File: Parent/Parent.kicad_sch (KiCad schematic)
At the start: 0 parts

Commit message: Worked on Parent - Move Workspace to cloud
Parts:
- added BT105, BT29, BT30, BT45, BT60, BT75, BT90: Battery_Cell, symbol Device:Battery_Cell
- added D1, D2, D3, D4, D5, D6, D7, D8: LED, symbol Device:LED
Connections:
- net Fuse Box/Lights Back Fused: now also D1.2 (A), D2.2 (A), D4.2 (A), D6.2 (A), D8.2 (A)
- net Fuse Box/Lights Front Fused: now also D3.2 (A), D5.2 (A), D7.2 (A)
- new net -BATT: BT29.2 (-)
- new net BMS_Passive1/Batt+: BT29.1 (+), BT30.2 (-)
- new net BMS_Passive2/Batt+: BT30.1 (+), BT45.2 (-)
- new net BMS_Passive3/Batt+: BT45.1 (+), BT60.2 (-)
- new net BMS_Passive4/Batt+: BT60.1 (+), BT75.2 (-)
- new net BMS_Passive5/Batt+: BT75.1 (+), BT90.2 (-)
- new net BMS_Passive6/Batt+: BT105.2 (-), BT90.1 (+)
- new net BMS_Passive7/Batt+: BT105.1 (+)
- new net Lights Controller/BrakeDrain_{S0}: D1.1 (K)
- new net Lights Controller/BrakeDrain_{S1}: D2.1 (K)
- new net Lights Controller/HazzardDrain_{L}: D5.1 (K), D6.1 (K)
- new net Lights Controller/HazzardDrain_{R}: D7.1 (K), D8.1 (K)
- new net Lights Controller/MainDrain: D3.1 (K), D4.1 (K)
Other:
- removed sheet BMS
- added sheet BMS_Passive1 (BMS_Passive.kicad_sch)
- added sheet BMS_Passive2 (BMS_Passive.kicad_sch)
- added sheet BMS_Passive3 (BMS_Passive.kicad_sch)
- added sheet BMS_Passive4 (BMS_Passive.kicad_sch)
- added sheet BMS_Passive5 (BMS_Passive.kicad_sch)
- added sheet BMS_Passive6 (BMS_Passive.kicad_sch)
- added sheet BMS_Passive7 (BMS_Passive.kicad_sch)
- added sheet Battery Charger (BatteryCharger.kicad_sch)
- added sheet Fault Logic Controller (FaultLogicController.kicad_sch)
- added sheet Level Translator1 (LevelTranslator.kicad_sch)
- added sheet Level Translator2 (LevelTranslator.kicad_sch)
- added sheet Level Translator3 (LevelTranslator.kicad_sch)
- added sheet Level Translator4 (LevelTranslator.kicad_sch)
- added sheet Level Translator5 (LevelTranslator.kicad_sch)
- added sheet Level Translator6 (LevelTranslator.kicad_sch)
- added sheet Level Translator7 (LevelTranslator.kicad_sch)
- added sheet Lights Controller (Light Controller.kicad_sch)
- sheet Fuse Box ports: added Battery Charger ; removed none
- note added: "Battery Charger"

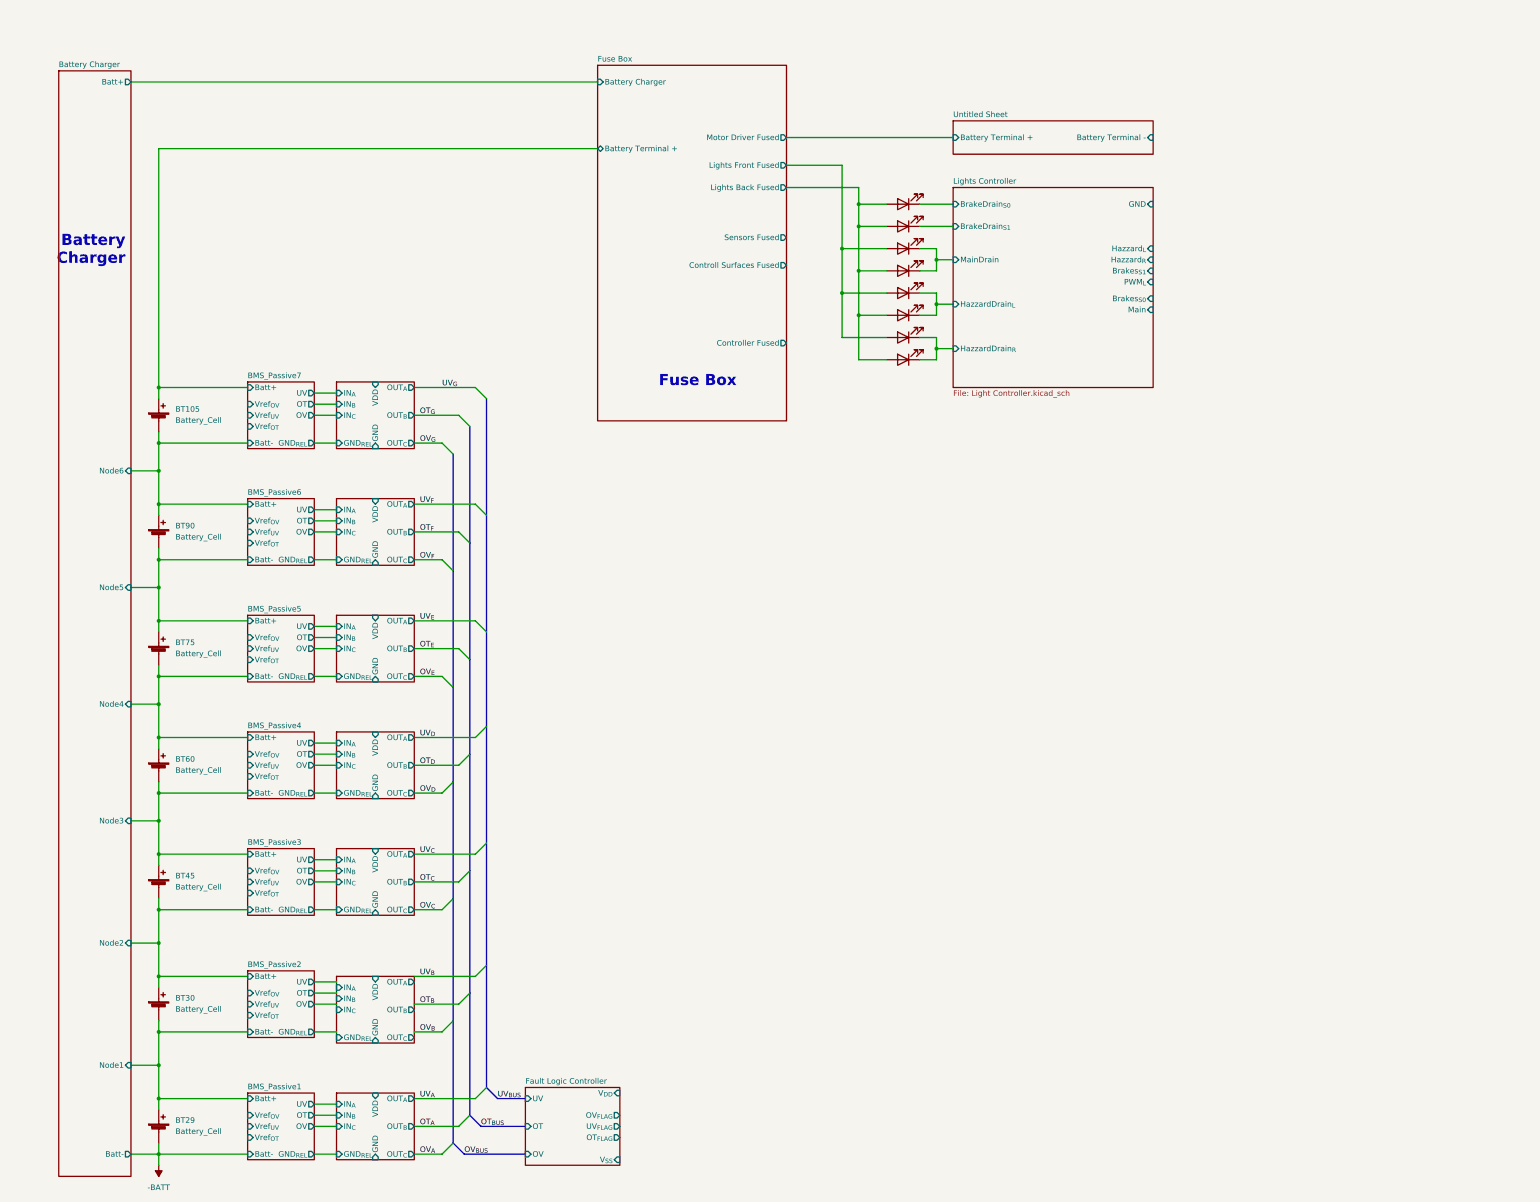
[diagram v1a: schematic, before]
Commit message: Updated Parent further - Move workspace to cloud
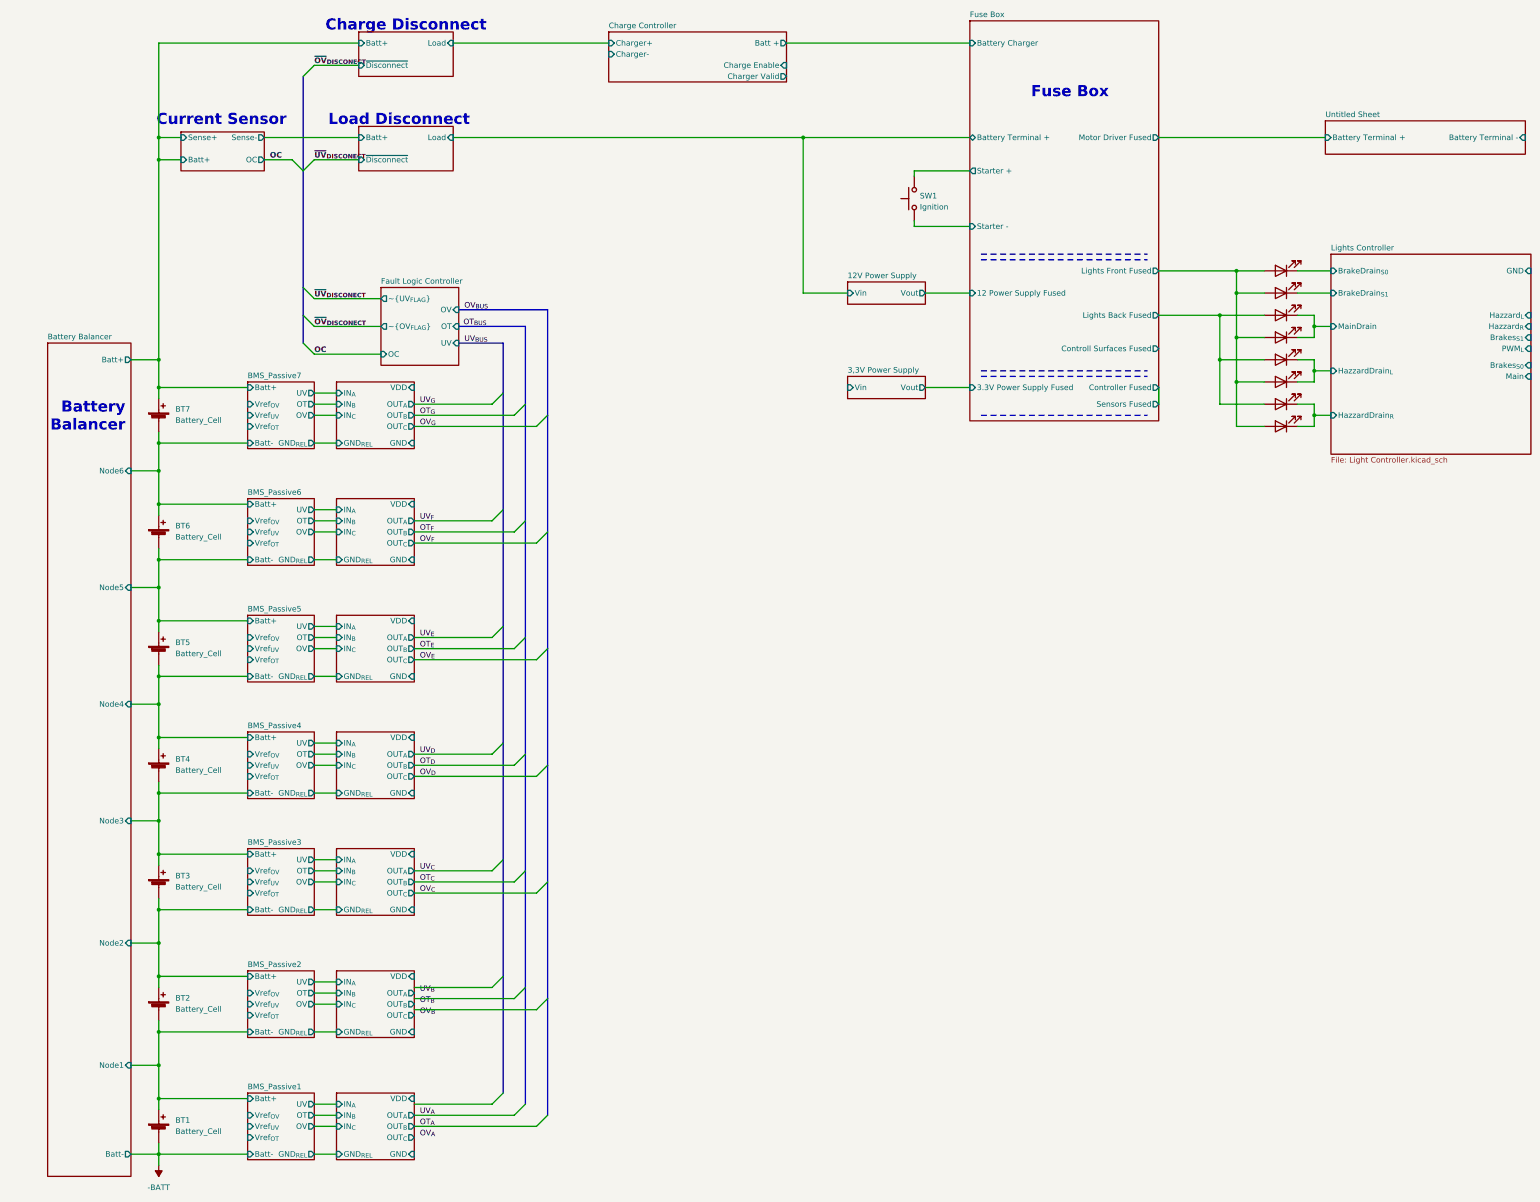
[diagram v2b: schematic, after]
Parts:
- added SW1: Ignition, symbol Switch:SW_Push
- renumbered BT29 to BT1, BT30 to BT2, BT45 to BT3, BT60 to BT4, BT75 to BT5, BT90 to BT6, BT105 to BT7
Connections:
- net Fuse Box/Lights Back Fused: now also D3.2 (A), D5.2 (A), D7.2 (A); no longer D1.2 (A), D2.2 (A), D4.2 (A), D6.2 (A), D8.2 (A)
- net Fuse Box/Lights Front Fused: now also D1.2 (A), D2.2 (A), D4.2 (A), D6.2 (A), D8.2 (A); no longer D3.2 (A), D5.2 (A), D7.2 (A)
- new net Fuse Box/Starter +: SW1.2
- new net Fuse Box/Starter -: SW1.1
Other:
- sheet Battery Charger renamed Battery Balancer
- added sheet 12V Power Supply (12V_PowerSupply.kicad_sch)
- added sheet 3,3V Power Supply (3.3V_PowerSupply.kicad_sch)
- added sheet Charge Controller (ChargeController.kicad_sch)
- added sheet Disconnect  (LoadStop_sch.kicad_sch)
- added sheet Overcurrent Detection (OvercurrentDetection.kicad_sch)
- sheet Fault Logic Controller ports: added OC, ~{OV_{FLAG}}, ~{UV_{FLAG}}; removed OT_{FLAG}, OV_{FLAG}, UV_{FLAG}, V_{DD}, V_{SS}
- sheet Fuse Box ports: added 12 Power Supply Fused, 3.3V Power Supply Fused, Starter +, Starter -; removed none
- note added: "Battery Balancer"
- note added: "Charge Disconnect"
- note added: "Current Sensor"
- note added: "Load Disconnect"
- note removed: "Battery Charger"

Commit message: Updated Parent further - Move workspace to cloud
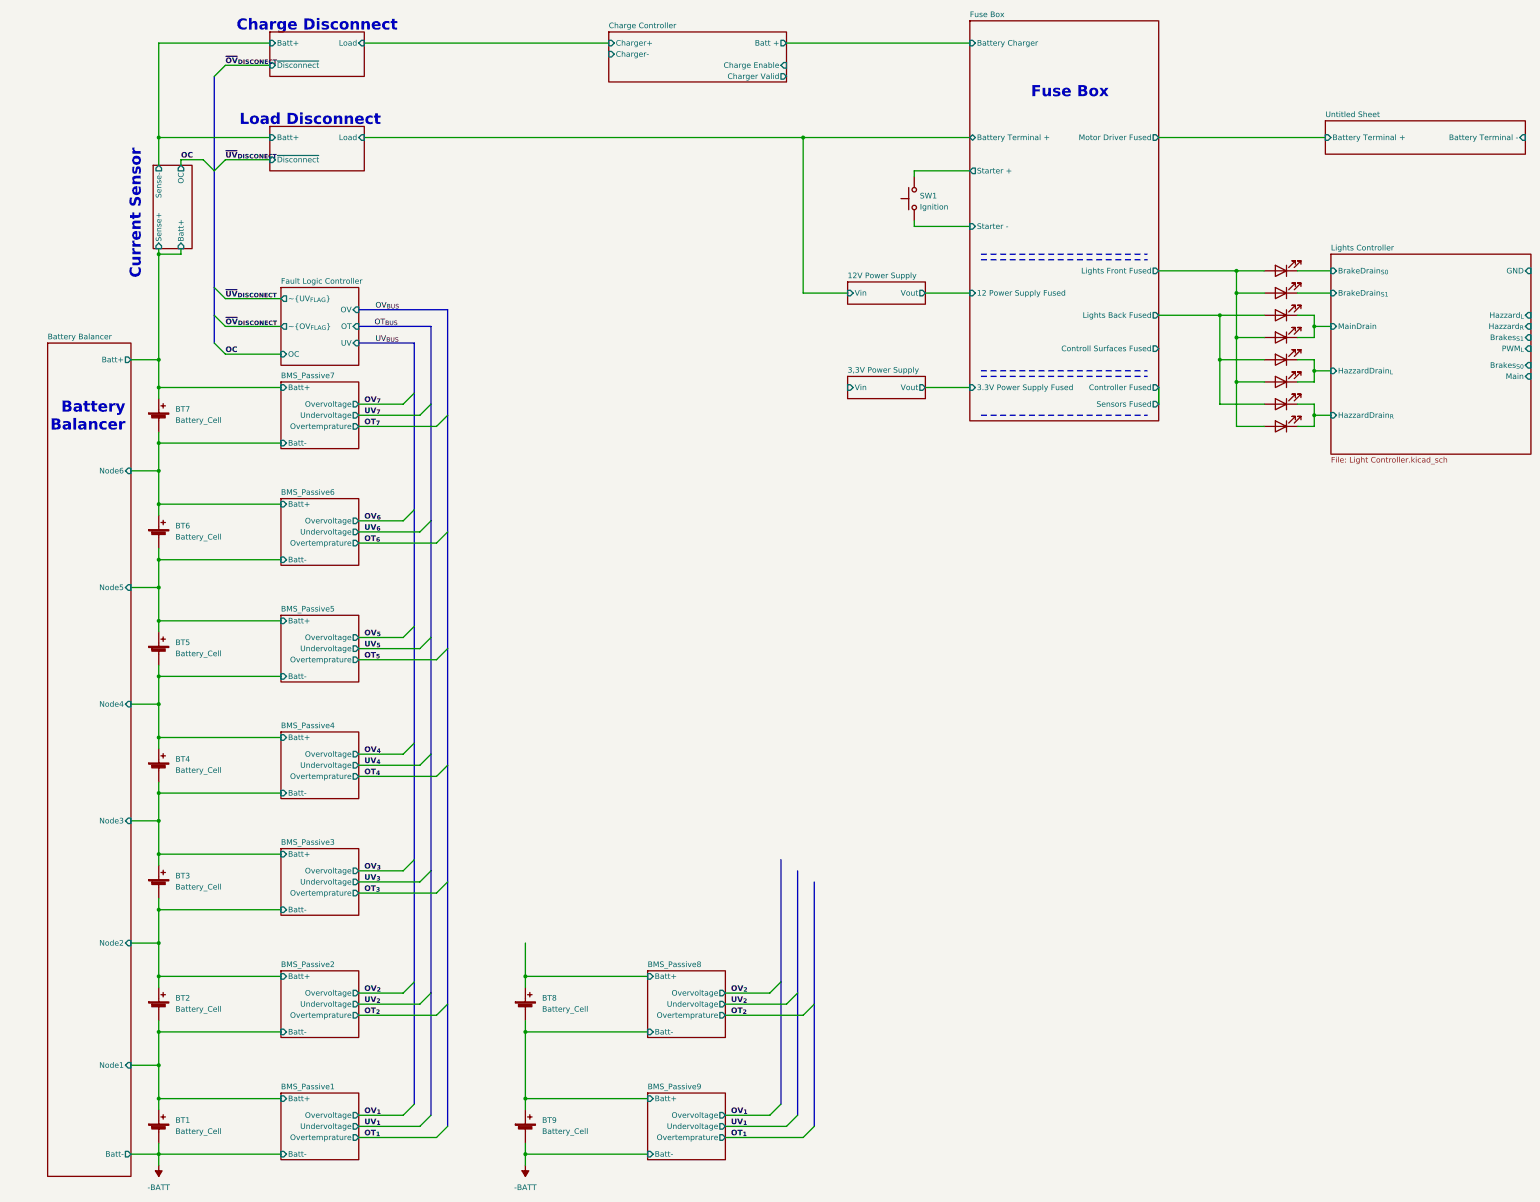
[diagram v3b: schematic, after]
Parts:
- added BT8, BT9: Battery_Cell, symbol Device:Battery_Cell
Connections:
- net -BATT: now also BT9.2 (-)
- new net BMS_Passive8/Batt+: BT8.1 (+)
- new net BMS_Passive8/Batt-: BT8.2 (-), BT9.1 (+)
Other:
- removed sheet Level Translator1
- removed sheet Level Translator2
- removed sheet Level Translator3
- removed sheet Level Translator4
- removed sheet Level Translator5
- removed sheet Level Translator6
- removed sheet Level Translator7
- added sheet BMS_Passive8 (BMS_Passive.kicad_sch)
- added sheet BMS_Passive9 (BMS_Passive.kicad_sch)
- sheet BMS_Passive1 ports: added Overtemprature, Overvoltage, Undervoltage; removed GND_{REL}, OT, OV, UV, Vref_{OT}, Vref_{OV}, Vref_{UV}
- sheet BMS_Passive2 ports: added Overtemprature, Overvoltage, Undervoltage; removed GND_{REL}, OT, OV, UV, Vref_{OT}, Vref_{OV}, Vref_{UV}
- sheet BMS_Passive3 ports: added Overtemprature, Overvoltage, Undervoltage; removed GND_{REL}, OT, OV, UV, Vref_{OT}, Vref_{OV}, Vref_{UV}
- sheet BMS_Passive4 ports: added Overtemprature, Overvoltage, Undervoltage; removed GND_{REL}, OT, OV, UV, Vref_{OT}, Vref_{OV}, Vref_{UV}
- sheet BMS_Passive5 ports: added Overtemprature, Overvoltage, Undervoltage; removed GND_{REL}, OT, OV, UV, Vref_{OT}, Vref_{OV}, Vref_{UV}
- sheet BMS_Passive6 ports: added Overtemprature, Overvoltage, Undervoltage; removed GND_{REL}, OT, OV, UV, Vref_{OT}, Vref_{OV}, Vref_{UV}
- sheet BMS_Passive7 ports: added Overtemprature, Overvoltage, Undervoltage; removed GND_{REL}, OT, OV, UV, Vref_{OT}, Vref_{OV}, Vref_{UV}

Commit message: Updated Parent - Moved workspace to cloud
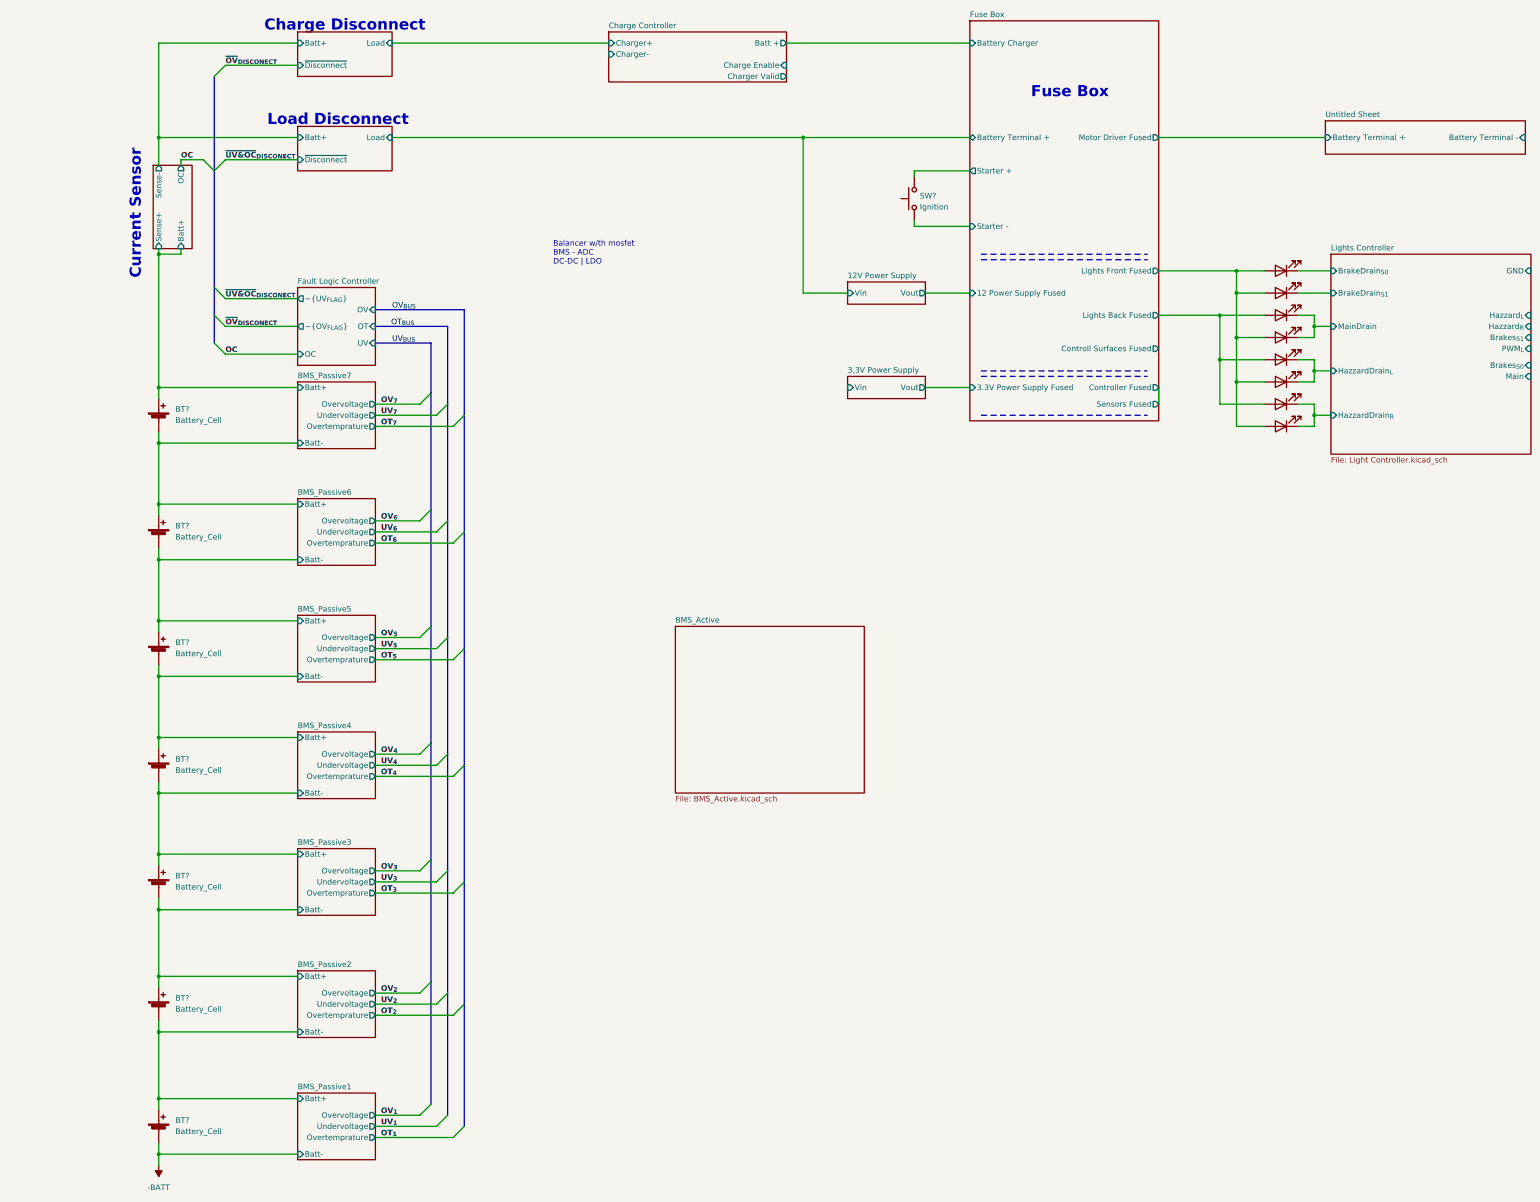
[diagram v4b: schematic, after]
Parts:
- removed BT8, BT9: Battery_Cell, symbol Device:Battery_Cell
- renumbered BT3 to BT?, BT6 to BT?, BT2 to BT?, BT5 to BT?, BT7 to BT?, BT1 to BT?, BT4 to BT?, D8 to D?, D1 to D?, D5 to D?, D4 to D?, D6 to D?, D3 to D?, D2 to D?, D7 to D?, SW1 to SW?
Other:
- removed sheet BMS_Passive8
- removed sheet BMS_Passive9
- removed sheet Battery Balancer
- added sheet BMS_Active (BMS_Active.kicad_sch)
- note added: "Balancer w/th mosfet BMS - ADC DC-DC | LDO"
- note removed: "Battery Balancer"
